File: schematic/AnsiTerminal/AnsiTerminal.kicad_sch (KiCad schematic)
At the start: 36 parts, among them J1 VGA_Output, J13 ManageDTR, J2 RS232

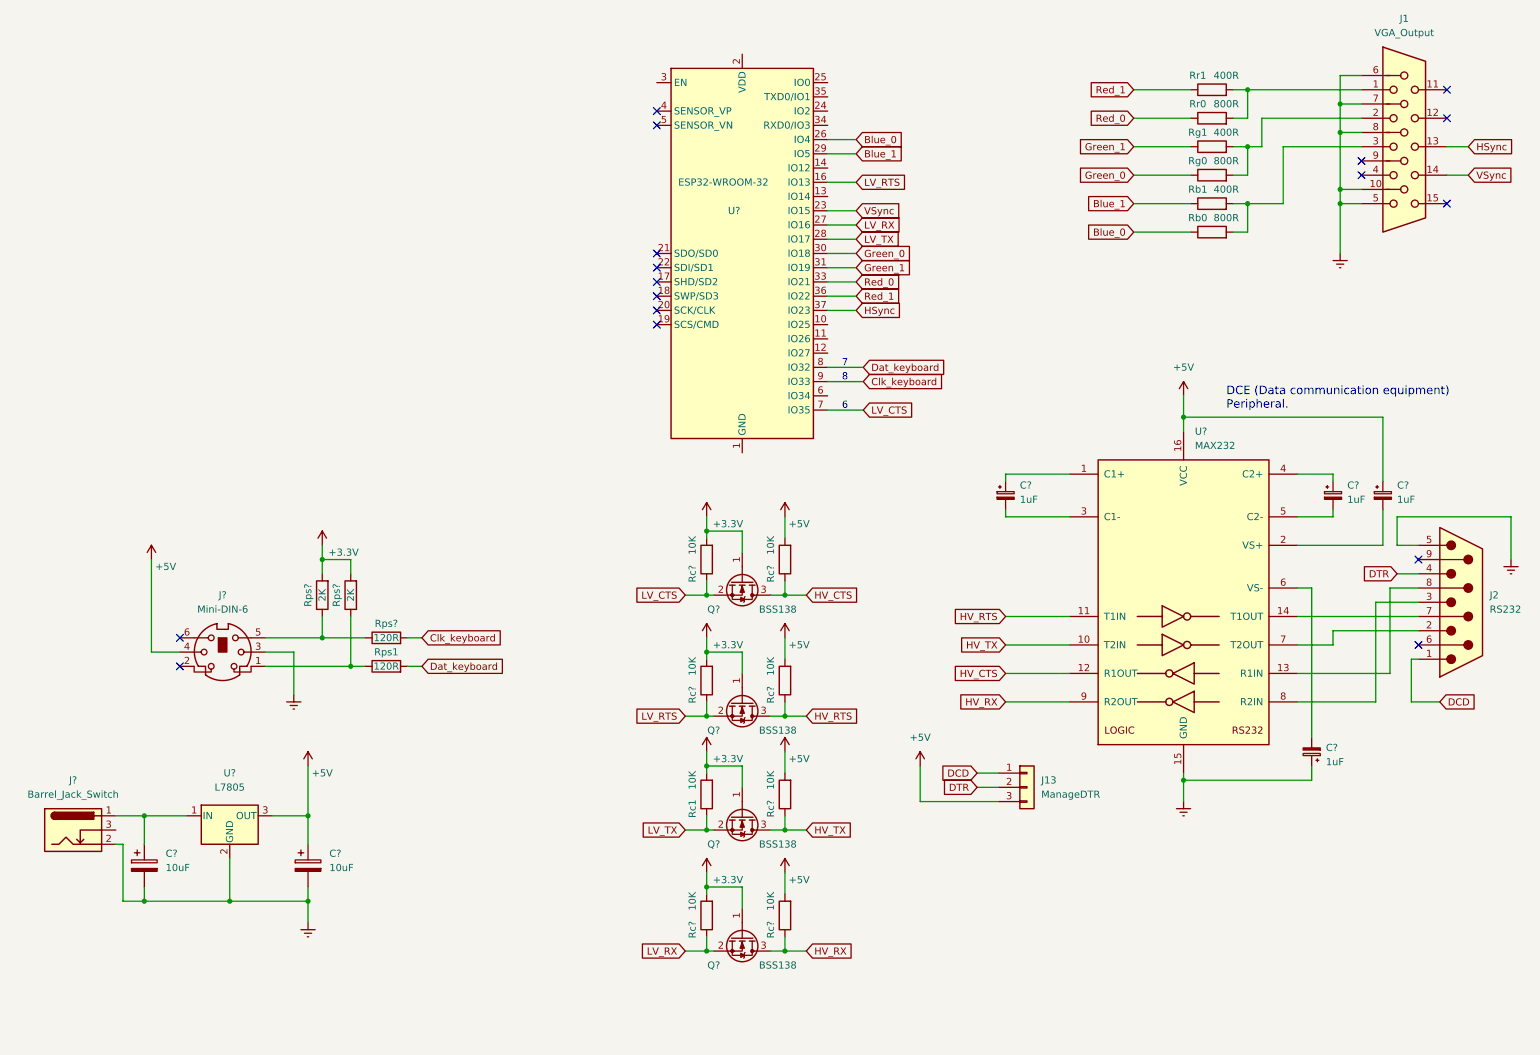
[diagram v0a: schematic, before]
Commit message: fixed max232 cap acitor pin 2 was inverted
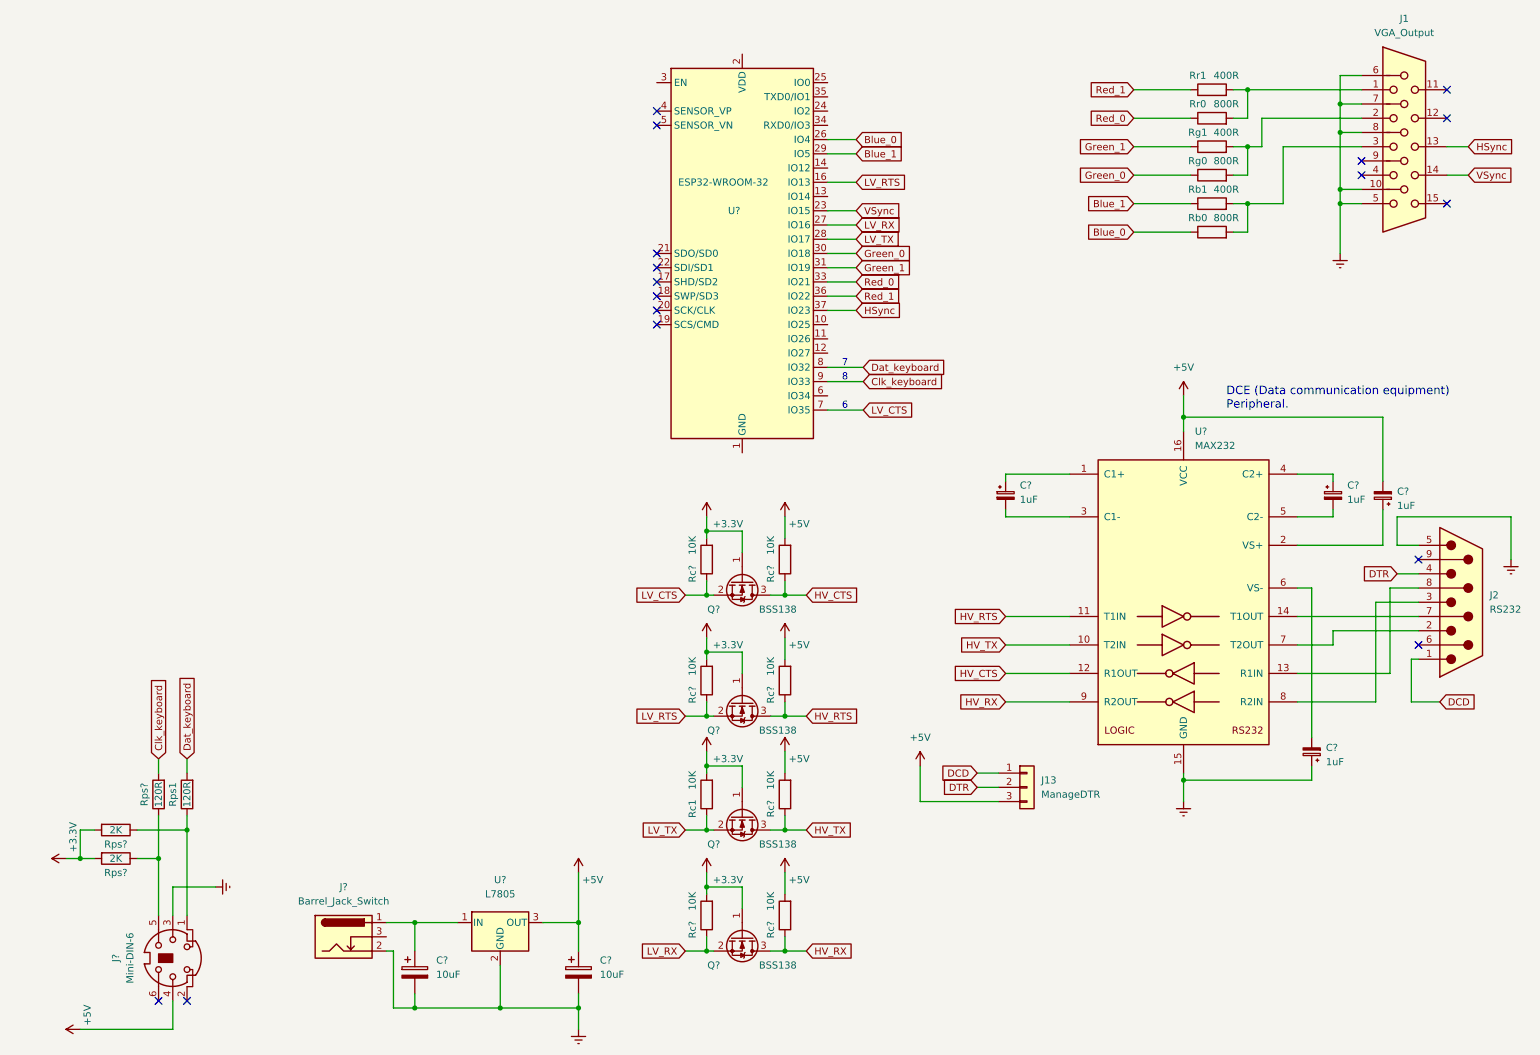
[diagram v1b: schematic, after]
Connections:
- net +5V: now also C?.2; no longer C?.1
- net at U?.2 (VS+): now also C?.1; no longer C?.2
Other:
- moved on the sheet: C?, J?, Rps1, Rps?, U?

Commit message: Fixed: The TX pin goes directly from the CPU to the RS232 chip
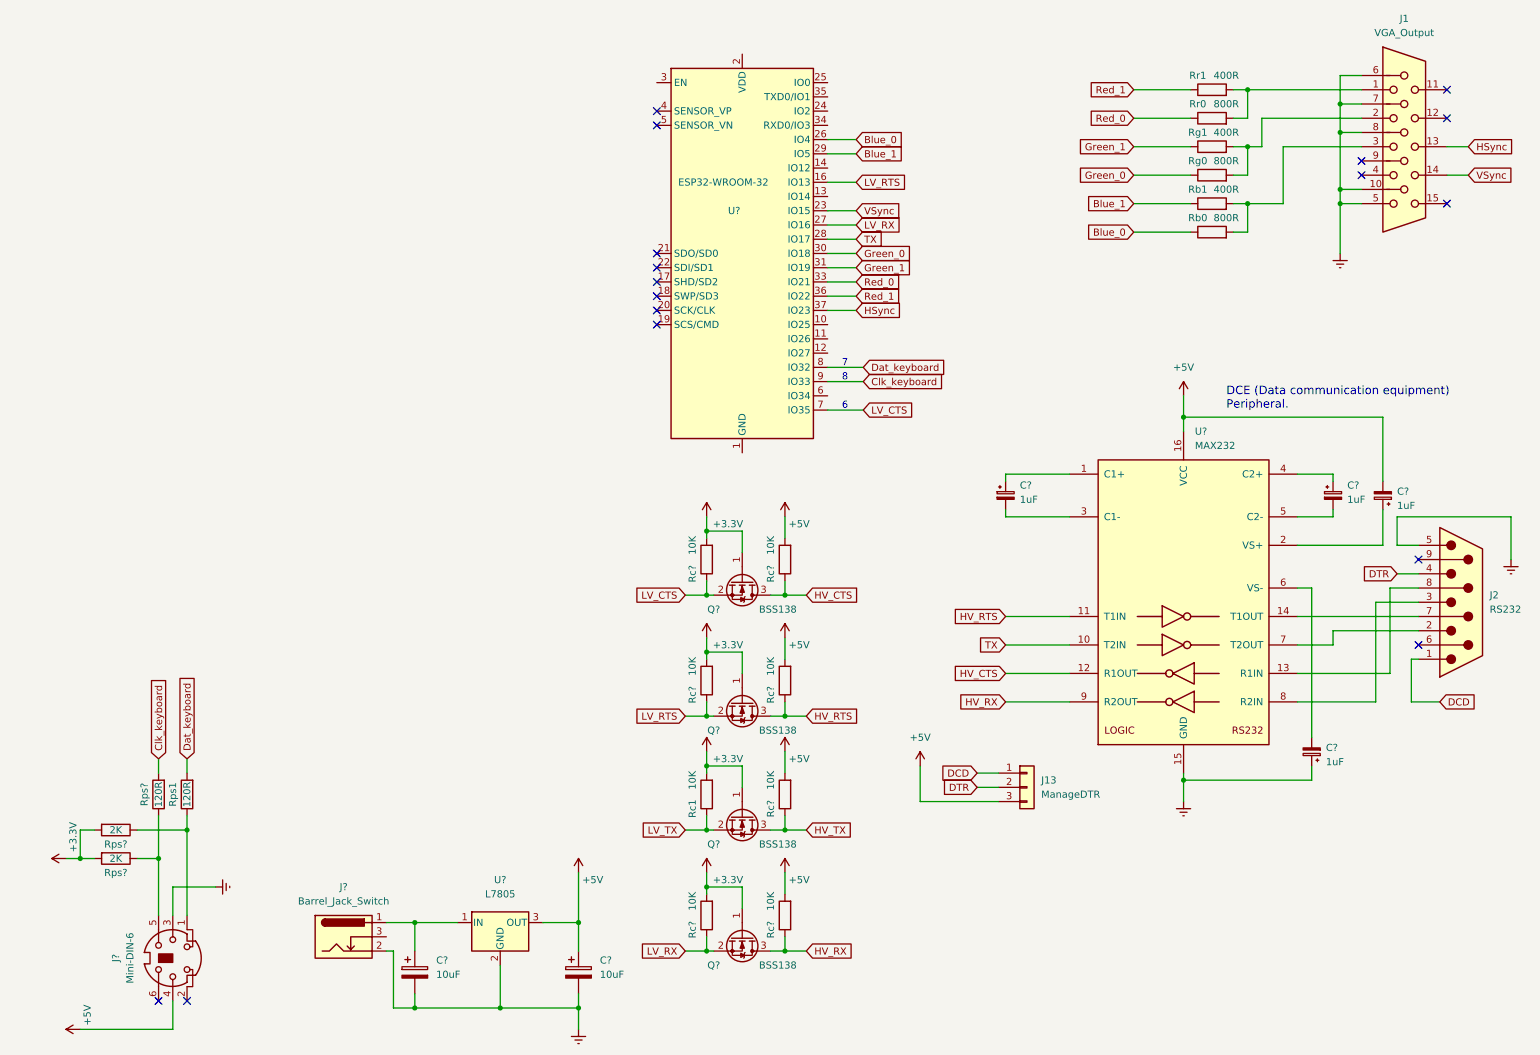
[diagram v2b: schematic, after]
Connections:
- net HV_TX: no longer U?.10 (T2IN)
- net LV_TX: no longer U?.28 (IO17)
- new net TX: U?.10 (T2IN), U?.28 (IO17)

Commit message: Versao 1.0.00
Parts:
- added Q1, Q2: NPN, symbol Simulation_SPICE:NPN
- added SW1 (x2): SW_DIP_x06, symbol Switch:SW_DIP_x06
- gave numbers to parts that had none: 2
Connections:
- net Clk_keyboard: now also Q2.1 (C)
- net Dat_keyboard: now also Q1.1 (C)
- net GNDREF: now also Q1.3 (E), Q2.3 (E), SW1.10, SW1.11, SW1.12, SW1.7, SW1.8, SW1.9
- net at U?.11 (IO26): now also Q2.2 (B)
- net at U?.12 (IO27): now also Q1.2 (B)
- net at U?.13 (IO14): now also SW1.2
- net at U?.14 (IO12): now also SW1.1
- net HV_TX renamed Livre1
- net LV_TX renamed livre2
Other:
- note added: "10"
- note added: "11"
- note added: "12"
- note added: "13"
- moved on the sheet: U?
